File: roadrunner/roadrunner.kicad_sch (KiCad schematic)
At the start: 86 parts, among them J1 Battery_conn, J2 battery_conn_r, J3 track_point_left, J4 niceview_left, J5 niceview_right, J6 track_point_right, J7 VIK_Left, J8 VIK_Right, SW1 SW_Push, SW10 SW_Push, SW10_r1 SW_Push, SW11 SW_Push, SW11_r1 SW_Push, SW12 SW_Push, SW12_r1 SW_Push, SW13 SW_Push, SW13_r1 SW_Push, SW14 SW_Push, SW14_r1 SW_Push, SW15 SW_Push, SW15_r1 SW_Push, SW16 SW_Push, SW16_r1 SW_Push, SW17 SW_Push, SW17_r1 SW_Push, SW1_r1 SW_Push, SW2 SW_Push, SW2_r1 SW_Push, SW3 SW_Push, SW3_r1 SW_Push, SW4 SW_Push, SW4_r1 SW_Push, SW5 SW_Push, SW5_r1 SW_Push, SW6 SW_Push, SW6_r1 SW_Push, SW7 SW_Push, SW7_r1 SW_Push, SW8 SW_Push, SW8_r1 SW_Push, SW9 SW_Push, SW9_r1 SW_Push, U1 ProMicro-kbd, U2 ProMicro-kbd

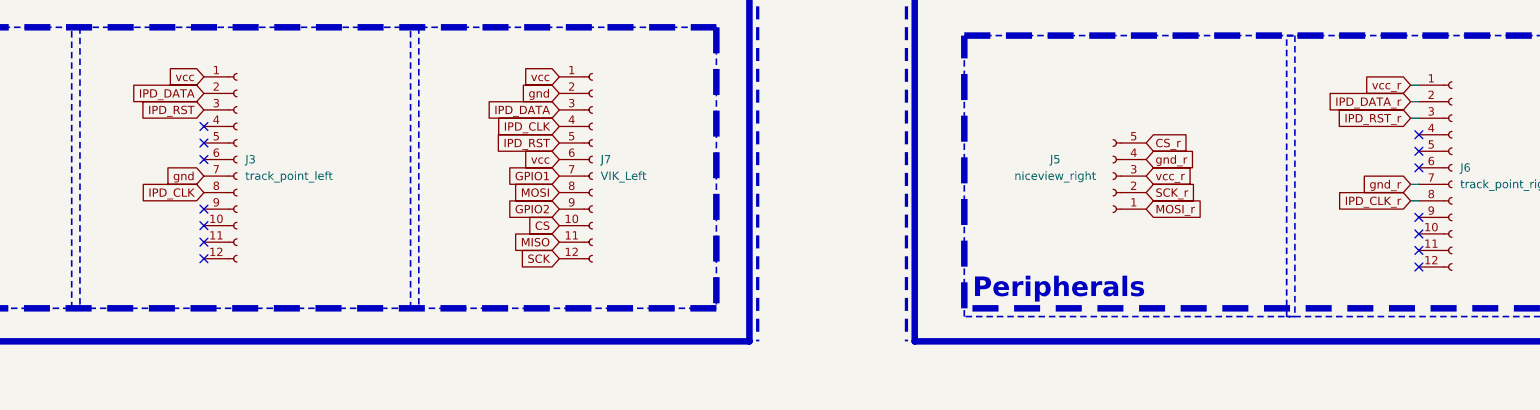
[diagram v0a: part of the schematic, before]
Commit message: feat: make track-point connector reversible
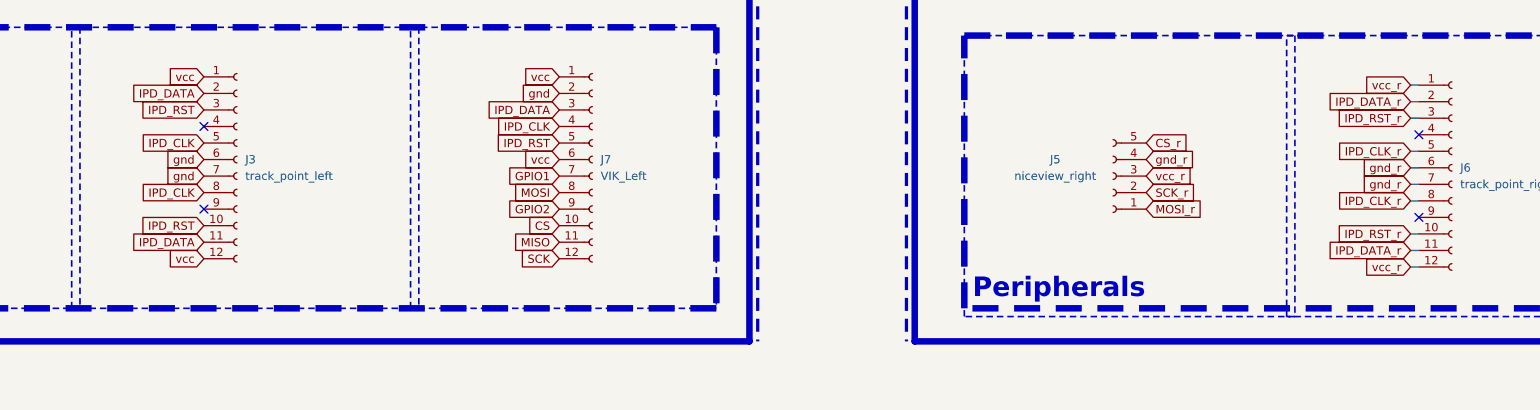
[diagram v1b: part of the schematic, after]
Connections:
- net IPD_CLK: now also J3.5 (Pin_5)
- net IPD_CLK_r: now also J6.5 (Pin_5)
- net IPD_DATA: now also J3.11 (Pin_11)
- net IPD_DATA_r: now also J6.11 (Pin_11)
- net IPD_RST: now also J3.10 (Pin_10)
- net IPD_RST_r: now also J6.10 (Pin_10)
- net gnd: now also J3.6 (Pin_6)
- net gnd_r: now also J6.6 (Pin_6)
- net vcc: now also J3.12 (Pin_12)
- net vcc_r: now also J6.12 (Pin_12)
- no-connect marks 14 -> 4
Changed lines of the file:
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@@
   )
   (no_connect (at 280.67 191.77))
-  (no_connect (at 93.98 208.28))
-  (no_connect (at 93.98 193.04))
-  (no_connect (at 93.98 195.58))
-  (no_connect (at 93.98 210.82))
-  (no_connect (at 93.98 205.74))
   (no_connect (at 93.98 190.5))
-  (no_connect (at 280.67 196.85))
   (no_connect (at 93.98 203.2))
   (no_connect (at 280.67 204.47))
-  (no_connect (at 280.67 207.01))
-  (no_connect (at 280.67 212.09))
-  (no_connect (at 280.67 194.31))
-  (no_connect (at 280.67 209.55))
   (wire (pts (xy 243.84 92.71) (xy 243.84 114.3))
     (stroke (width 0) (type default))
@@
   )
   (wire (pts (xy 53.34 114.3) (xy 53.34 115.57))
+    (stroke (width 0) (type default))
+  )
+  (wire (pts (xy 279.4 194.31) (xy 280.67 194.31))
     (stroke (width 0) (type default))
   )
@@
     (stroke (width 0) (type default))
   )
+  (wire (pts (xy 279.4 196.85) (xy 280.67 196.85))
+    (stroke (width 0) (type default))
+  )
   (wire (pts (xy 260.35 133.35) (xy 261.62 133.35))
     (stroke (width 0) (type default))
@@
     (stroke (width 0) (type default))
   )
+  (wire (pts (xy 279.4 209.55) (xy 280.67 209.55))
+    (stroke (width 0) (type default))
+  )
   (wire (pts (xy 243.84 114.3) (xy 243.84 133.35))
     (stroke (width 0) (type default))
@@
     (stroke (width 0) (type default))
   )
+  (wire (pts (xy 279.4 207.01) (xy 280.67 207.01))
+    (stroke (width 0) (type default))
+  )
   (wire (pts (xy 238.76 144.78) (xy 223.52 144.78))
     (stroke (width 0) (type default))
@@
     (stroke (width 0) (type default))
   )
+  (wire (pts (xy 279.4 212.09) (xy 280.67 212.09))
+    (stroke (width 0) (type default))
+  )
   (wire (pts (xy 256.54 101.6) (xy 256.54 104.14))
     (stroke (width 0) (type default))
@@
     )
   )
+  (global_label "gnd" (shape input) (at 93.98 195.58 180) (fields_autoplaced)
+    (effects (font (size 1.27 1.27)) (justify right))
+    (property "Intersheetrefs" "${INTERSHEET_REFS}" (at 288.29 233.68 0)
+      (effects (font (size 1.27 1.27)) hide)
+    )
+  )
   (global_label "IPD_DATA_r" (shape input) (at 236.22 46.99 180) (fields_autoplaced)
     (effects (font (size 1.27 1.27)) (justify right))
@@
     )
   )
+  (global_label "IPD_DATA_r" (shape input) (at 279.4 209.55 180) (fields_autoplaced)
+    (effects (font (size 1.27 1.27)) (justify right))
+    (property "Intersheetrefs" "${INTERSHEET_REFS}" (at 266.1338 209.55 0)
+      (effects (font (size 1.27 1.27)) (justify right) hide)
+    )
+  )
   (global_label "IPD_DATA_r" (shape input) (at 279.4 186.69 180) (fields_autoplaced)
     (effects (font (size 1.27 1.27)) (justify right))
@@
     )
   )
+  (global_label "IPD_RST" (shape input) (at 93.98 205.74 180) (fields_autoplaced)
+    (effects (font (size 1.27 1.27)) (justify right))
+    (property "Intersheetrefs" "${INTERSHEET_REFS}" (at 84.0074 205.6606 0)
+      (effects (font (size 1.27 1.27)) (justify right) hide)
+    )
+  )
   (global_label "GPIO1" (shape input) (at 78.74 45.72 0) (fields_autoplaced)
     (effects (font (size 1.27 1.27)) (justify left))
@@
     )
   )
+  (global_label "vcc_r" (shape input) (at 279.4 212.09 180) (fields_autoplaced)
+    (effects (font (size 1.27 1.27)) (justify right))
+    (property "Intersheetrefs" "${INTERSHEET_REFS}" (at 271.5162 212.09 0)
+      (effects (font (size 1.27 1.27)) (justify right) hide)
+    )
+  )
   (global_label "ROW1" (shape input) (at 45.72 53.34 180) (fields_autoplaced)
     (effects (font (size 1.27 1.27)) (justify right))
@@
     )
   )
+  (global_label "vcc" (shape input) (at 93.98 210.82 180) (fields_autoplaced)
+    (effects (font (size 1.27 1.27)) (justify right))
+    (property "Intersheetrefs" "${INTERSHEET_REFS}" (at 288.29 254 0)
+      (effects (font (size 1.27 1.27)) hide)
+    )
+  )
+  (global_label "IPD_RST_r" (shape input) (at 279.4 207.01 180) (fields_autoplaced)
+    (effects (font (size 1.27 1.27)) (justify right))
+    (property "Intersheetrefs" "${INTERSHEET_REFS}" (at 267.1015 207.01 0)
+      (effects (font (size 1.27 1.27)) (justify right) hide)
+    )
+  )
   (global_label "vcc_r" (shape input) (at 266.7 39.37 0) (fields_autoplaced)
     (effects (font (size 1.27 1.27)) (justify left))
@@
     )
   )
+  (global_label "IPD_CLK_r" (shape input) (at 279.4 194.31 180) (fields_autoplaced)
+    (effects (font (size 1.27 1.27)) (justify right))
+    (property "Intersheetrefs" "${INTERSHEET_REFS}" (at 266.9805 194.31 0)
+      (effects (font (size 1.27 1.27)) (justify right) hide)
+    )
+  )
   (global_label "gnd" (shape input) (at 144.78 41.91 180) (fields_autoplaced)
     (effects (font (size 1.27 1.27)) (justify right))
@@
     )
   )
+  (global_label "IPD_DATA" (shape input) (at 93.98 208.28 180) (fields_autoplaced)
+    (effects (font (size 1.27 1.27)) (justify right))
+    (property "Intersheetrefs" "${INTERSHEET_REFS}" (at 83.0398 208.2006 0)
+      (effects (font (size 1.27 1.27)) (justify right) hide)
+    )
+  )
   (global_label "ROW2" (shape input) (at 33.02 146.05 180) (fields_autoplaced)
     (effects (font (size 1.27 1.27)) (justify right))
@@
     )
   )
+  (global_label "IPD_CLK" (shape input) (at 93.98 193.04 180) (fields_autoplaced)
+    (effects (font (size 1.27 1.27)) (justify right))
+    (property "Intersheetrefs" "${INTERSHEET_REFS}" (at 83.8864 192.9606 0)
+      (effects (font (size 1.27 1.27)) (justify right) hide)
+    )
+  )
   (global_label "CS_r" (shape input) (at 236.22 31.75 180) (fields_autoplaced)
     (effects (font (size 1.27 1.27)) (justify right))
@@
       (effects (font (size 1.27 1.27)) (justify right) hide)
     )
+  )
+  (global_label "gnd_r" (shape input) (at 279.4 196.85 180) (fields_autoplaced)
+    (effects (font (size 1.27 1.27)) (justify right))
+    (property "Intersheetrefs" "${INTERSHEET_REFS}" (at 271.214 196.85 0)
+      (effects (font (size 1.27 1.27)) (justify right) hide)
+    )
